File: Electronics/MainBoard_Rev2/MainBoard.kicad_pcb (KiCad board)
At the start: 2 copper layers, 57.2 x 35.1 mm, 70 parts, among them J1 Conn_01x04_Female, J2 DB9_Female, J3 USB_B_Micro, J4 Conn_01x04_Male, J5 Conn_01x02_Male, Q30 PMBT2222A, Q35 PMBT2222A, Q5 Q_NPN_BEC, Q6 Q_NPN_BEC, U1 ESP32-WROOM-32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

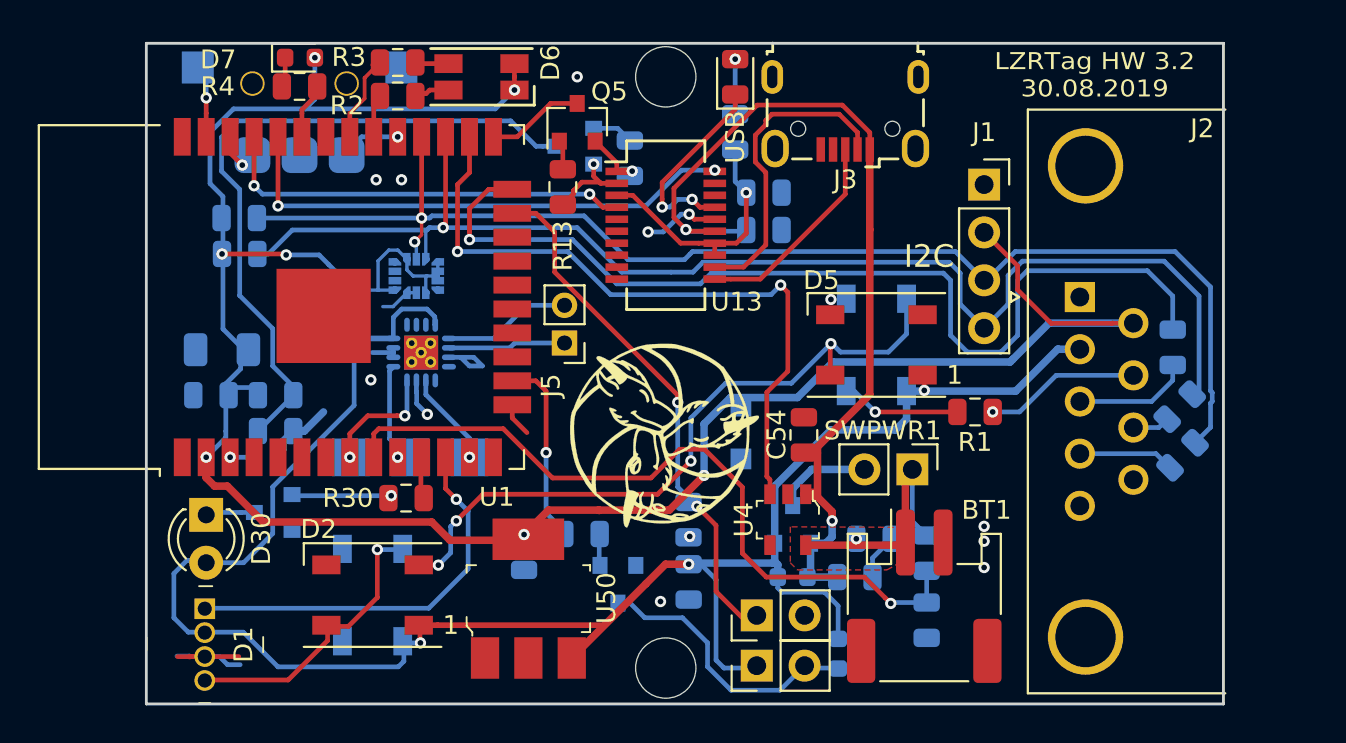
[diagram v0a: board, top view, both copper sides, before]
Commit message: Last changes for a functional Lasertag, ordered!
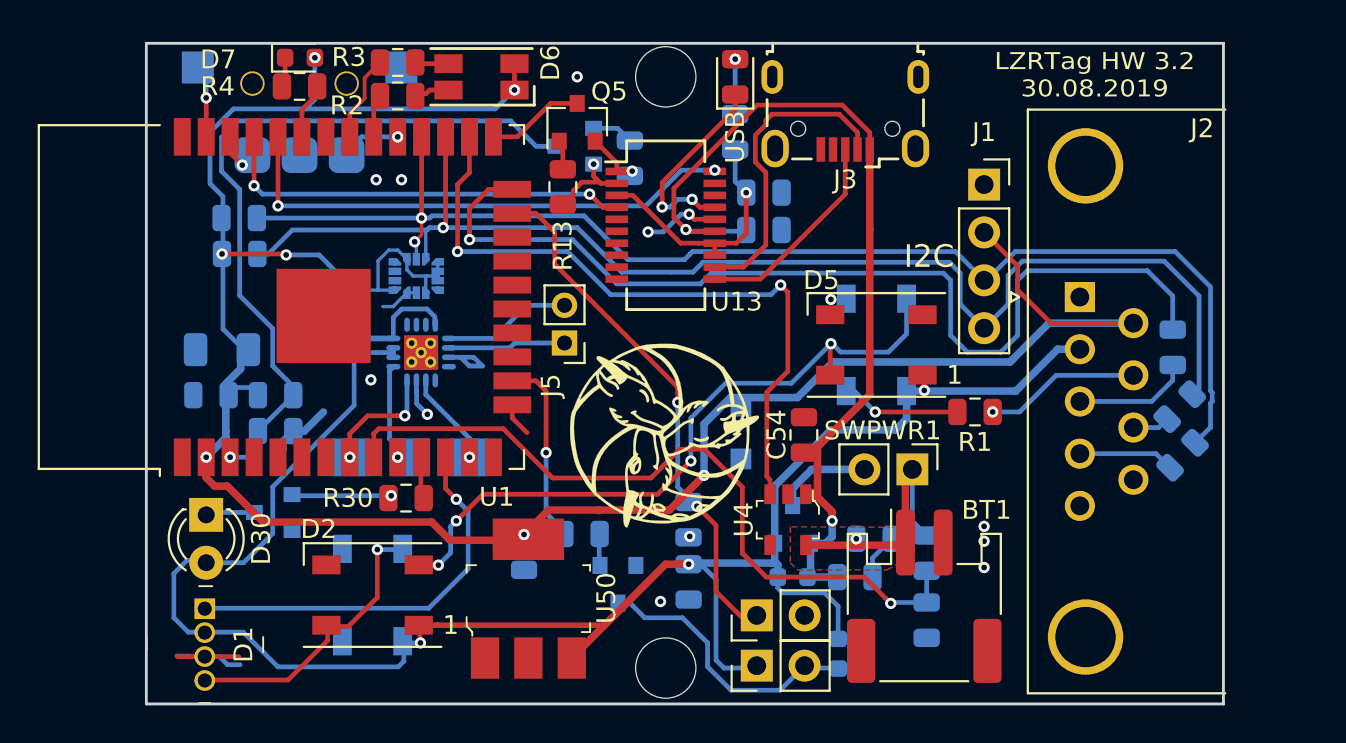
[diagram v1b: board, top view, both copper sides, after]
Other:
- rule trace_min: 0.2 -> 0.15
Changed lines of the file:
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@@
     (thickness 1.6)
     (drawings 17)
-    (tracks 581)
+    (tracks 583)
     (zones 0)
     (modules 70)
@@
     (zone_clearance 0.25)
     (zone_45_only yes)
-    (trace_min 0.2)
+    (trace_min 0.15)
     (segment_width 0.2)
     (edge_width 0.15)
@@
       (effects (font (size 0.5 0.5) (thickness 0.08)) (justify mirror))
     )
-    (pad 1 smd roundrect (at -0.9375 0 45) (size 0.975 1.4) (layers B.Cu B.Paste B.Mask) (roundrect_rratio 0.25)
+    (pad 1 smd roundrect (at -0.937501 0 45) (size 0.975 1.4) (layers B.Cu B.Paste B.Mask) (roundrect_rratio 0.25)
       (net 83 "Net-(J2-Pad4)"))
-    (pad 2 smd roundrect (at 0.9375 0 45) (size 0.975 1.4) (layers B.Cu B.Paste B.Mask) (roundrect_rratio 0.25)
+    (pad 2 smd roundrect (at 0.937501 0 45) (size 0.975 1.4) (layers B.Cu B.Paste B.Mask) (roundrect_rratio 0.25)
       (net 53 SCL))
     (model ${KISYS3DMOD}/Resistor_SMD.3dshapes/R_0805_2012Metric.wrl
@@
   (via (at 72.441 80.01) (size 0.6) (drill 0.3) (layers F.Cu B.Cu) (net 5))
   (segment (start 67.7165 97.3075) (end 67.7165 98.425) (width 0.25) (layer B.Cu) (net 5))
-  (segment (start 67.7165 98.425) (end 67.7165 99.822) (width 0.25) (layer B.Cu) (net 5))
+  (segment (start 67.7165 98.425) (end 67.7165 99.822) (width 0.4) (layer B.Cu) (net 5))
+  (segment (start 67.7165 99.822) (end 67.7165 100.1685) (width 0.4) (layer B.Cu) (net 5))
+  (segment (start 67.7165 100.1685) (end 66.675 101.21) (width 0.4) (layer B.Cu) (net 5))
   (segment (start 67.9195 97.5105) (end 69.215 97.5105) (width 0.25) (layer B.Cu) (net 5))
   (segment (start 67.7165 97.3075) (end 67.9195 97.5105) (width 0.25) (layer B.Cu) (net 5))
-  (segment (start 67.7165 100.1685) (end 66.675 101.21) (width 0.25) (layer B.Cu) (net 5))
-  (segment (start 67.7165 99.822) (end 67.7165 100.1685) (width 0.25) (layer B.Cu) (net 5))
   (segment (start 114.73863 94.095) (end 114.72663 94.107) (width 0.25) (layer F.Cu) (net 5))
   (segment (start 115.87 94.095) (end 114.73863 94.095) (width 0.25) (layer F.Cu) (net 5))
@@
   (segment (start 68.1228 82.7278) (end 71.9328 82.7278) (width 0.25) (layer B.Cu) (net 5))
   (segment (start 66.8782 83.9724) (end 68.1228 82.7278) (width 0.25) (layer B.Cu) (net 5))
-  (segment (start 67.7165 97.3075) (end 68.5038 96.5202) (width 0.25) (layer B.Cu) (net 5))
+  (segment (start 67.7165 97.3075) (end 68.5038 96.5202) (width 0.4) (layer B.Cu) (net 5))
+  (segment (start 68.5038 96.5202) (end 68.5038 95.343399) (width 0.4) (layer B.Cu) (net 5))
   (segment (start 68.5038 95.343399) (end 67.564 94.403599) (width 0.25) (layer B.Cu) (net 5))
   (segment (start 71.9328 82.7278) (end 72.441 82.2196) (width 0.25) (layer B.Cu) (net 5))
-  (segment (start 68.5038 96.5202) (end 68.5038 95.343399) (width 0.25) (layer B.Cu) (net 5))
   (segment (start 67.564 94.403599) (end 67.564 87.376) (width 0.25) (layer B.Cu) (net 5))
   (segment (start 71.9328 82.7278) (end 82.0166 82.7278) (width 0.25) (layer B.Cu) (net 5))
@@
   (segment (start 99.822 99.7585) (end 103.251 99.7585) (width 0.4) (layer B.Cu) (net 26))
   (segment (start 103.251 99.7585) (end 103.835 99.1745) (width 0.4) (layer B.Cu) (net 26))
-  (segment (start 100.203 109.093) (end 100.203 110.8455) (width 0.25) (layer B.Cu) (net 26))
-  (segment (start 97.0025 107.569) (end 97.0025 108.144) (width 0.25) (layer B.Cu) (net 26))
-  (segment (start 97.0025 108.144) (end 97.22751 108.36901) (width 0.25) (layer B.Cu) (net 26))
-  (segment (start 99.47901 108.36901) (end 100.203 109.093) (width 0.25) (layer B.Cu) (net 26))
-  (segment (start 97.22751 108.36901) (end 99.47901 108.36901) (width 0.25) (layer B.Cu) (net 26))
   (segment (start 93.726 111.971) (end 94.15 112.395) (width 0.25) (layer B.Cu) (net 26))
   (segment (start 92.274592 106.823447) (end 92.291039 106.807) (width 0.25) (layer B.Cu) (net 26))
@@
   (segment (start 91.0457 106.8855) (end 90.0081 107.9231) (width 0.4) (layer F.Cu) (net 26))
   (segment (start 92.274592 106.8855) (end 91.0457 106.8855) (width 0.4) (layer F.Cu) (net 26))
+  (segment (start 100.203 109.1184) (end 100.203 110.8455) (width 0.25) (layer B.Cu) (net 26))
+  (segment (start 99.67861 108.59401) (end 100.203 109.1184) (width 0.25) (layer B.Cu) (net 26))
+  (segment (start 99.67516 108.59401) (end 99.67861 108.59401) (width 0.25) (layer B.Cu) (net 26))
+  (segment (start 97.0025 107.569) (end 97.0025 108.144) (width 0.25) (layer B.Cu) (net 26))
+  (segment (start 97.0025 108.144) (end 97.2657 108.4072) (width 0.25) (layer B.Cu) (net 26))
+  (segment (start 97.2657 108.4072) (end 99.48835 108.4072) (width 0.25) (layer B.Cu) (net 26))
+  (segment (start 99.48835 108.4072) (end 99.67516 108.59401) (width 0.25) (layer B.Cu) (net 26))
   (segment (start 98.298 112.395) (end 100.1775 112.395) (width 0.25) (layer B.Cu) (net 27))
   (segment (start 97.122999 113.570001) (end 98.298 112.395) (width 0.25) (layer B.Cu) (net 27))
@@
   (segment (start 84.709 100.965) (end 84.709 104.1655) (width 0.25) (layer B.Cu) (net 39))
   (via (at 91.694 98.297992) (size 0.6) (drill 0.3) (layers F.Cu B.Cu) (net 40))
-  (segment (start 91.694 97.917) (end 91.694 98.297992) (width 0.25) (layer F.Cu) (net 40))
-  (segment (start 82.915 88.265) (end 84.165 88.265) (width 0.25) (layer F.Cu) (net 40))
-  (segment (start 84.165 88.265) (end 85.1662 89.2662) (width 0.25) (layer F.Cu) (net 40))
-  (segment (start 85.1662 89.2662) (end 85.1662 91.3892) (width 0.25) (layer F.Cu) (net 40))
-  (segment (start 85.1662 91.3892) (end 91.694 97.917) (width 0.25) (layer F.Cu) (net 40))
   (segment (start 91.694 98.297992) (end 91.694 102.793802) (width 0.25) (layer B.Cu) (net 40))
   (segment (start 91.694 102.793802) (end 92.410001 103.509803) (width 0.25) (layer B.Cu) (net 40))
@@
   (segment (start 93.726 108.331) (end 93.726 104.825802) (width 0.25) (layer F.Cu) (net 40))
   (segment (start 95.25 109.855) (end 93.726 108.331) (width 0.25) (layer F.Cu) (net 40))
+  (segment (start 91.694 97.4979) (end 91.694 98.297992) (width 0.25) (layer F.Cu) (net 40))
+  (segment (start 82.915 88.265) (end 84.165 88.265) (width 0.25) (layer F.Cu) (net 40))
+  (segment (start 85.1662 89.2662) (end 85.1662 90.9701) (width 0.25) (layer F.Cu) (net 40))
+  (segment (start 84.165 88.265) (end 85.1662 89.2662) (width 0.25) (layer F.Cu) (net 40))
+  (segment (start 85.1662 90.9701) (end 91.694 97.4979) (width 0.25) (layer F.Cu) (net 40))
   (segment (start 78.53 81.726) (end 78.341 81.915) (width 0.25) (layer F.Cu) (net 41))
   (segment (start 79.53 81.726) (end 78.53 81.726) (width 0.25) (layer F.Cu) (net 41))

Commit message: Modify board for the v3.3 release-ish
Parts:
- removed D35: D_Schottky, Diode_SMD:D_0603_1608Metric
- removed D6: LED_Dual_AACC, LED_SMD:LED_RGB_1210
- removed D7: LED, LED_SMD:LED_0603_1608Metric
- removed J2: DB9_Female, Connector_Dsub:DSUB-9_Female_Horizontal_P2.77x2.84mm_EdgePinOffset4.94mm_Housed_MountingHolesOffset7.48mm
- removed Q35: PMBT2222A, Package_TO_SOT_SMD:SOT-23
- removed R2, R3: 220R, Resistor_SMD:R_0805_2012Metric
- removed R35: 2.2k, Resistor_SMD:R_0805_2012Metric
- removed R4: 220, Resistor_SMD:R_0805_2012Metric
- added C201: 0.1uF, Capacitor_SMD:C_0805_2012Metric, F.Cu at (85.4, 101.3)
- added C401: 1uF, Capacitor_SMD:C_0805_2012Metric, B.Cu at (109.6, 102.3)
- added D401: IN-PI42TAS, XasPrints:IN-PI42TAS, F.Cu at (109.1, 80.8)
- added D402: IN-PI42TAS, XasPrints:IN-PI42TAS, F.Cu at (116.6, 80.9)
- added J101: 54602-908LF, Connector_RJ:RJ45_Amphenol_54602-x08_Horizontal, F.Cu at (111.0, 99.7)
- added U401: DRV2605, Package_SO:VSSOP-10_3x3mm_P0.5mm, B.Cu at (111.5, 107.2)
- BT1: footprint Connector_JST:JST_PH_S2B-PH-SM4-TB_1x02-1MP_P2.00mm_Horizontal -> Connector_PinHeader_2.54mm:PinHeader_1x02_P2.54mm_Horizontal; moved to B.Cu
- C2, C31, C8: value 150nF -> 100nF
- C3: value 0.1uF -> 100nF
- D1: footprint digikey-footprints:LED_RGB_WP154A4SUREQBFZGC -> Connector_PinHeader_2.00mm:PinHeader_1x04_P2.00mm_Vertical
- D30: value SFH4346 -> SFH4545; footprint LED_THT:LED_D3.0mm_IRBlack -> Connector_PinHeader_2.00mm:PinHeader_1x02_P2.00mm_Vertical
- R1: value 220 -> 220R; moved to B.Cu
- R13, R14: value R_Small -> 10k
- R30, R7, R8, R9: value 220 -> 220R
- R55: value 100k -> 50k
- R56: value 200k -> 50k; moved to F.Cu
- U3: value LSM6DS3 -> LSM6DSMTR
- moved H4 27.5 mm to (100.6, 83.9), turned to 0 degrees
- moved H3 22.2 mm to (87.4, 103.5)
- moved J1 19.9 mm to (116.6, 104.6)
- moved VBR1 17.9 mm to (113.7, 112.2), turned to 270 degrees
- moved R7 13.9 mm to (105.0, 90.5), turned to 180 degrees
- moved R8 11.3 mm to (111.3, 89.7), turned to 0 degrees
- moved R9 10.2 mm to (113.7, 92.0), turned to 0 degrees
- moved R1 7.52 mm to (113.7, 94.6), turned to 0 degrees
- moved R56 5.21 mm to (105.9, 104.7), turned to 0 degrees
- moved D1 4.72 mm to (65.2, 106.6), turned to 0 degrees
- moved D30 2.67 mm to (67.9, 106.6), turned to 0 degrees
- moved R55 1.83 mm to (105.9, 104.7), turned to 180 degrees
- moved BT1 1.26 mm to (103.9, 107.6), turned to 270 degrees
- moved H6 0.56 mm to (91.1, 99.5)
- moved SWPWR1 0.10 mm to (104.2, 101.9)
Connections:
- AMP1 pad 7: Net-(AMP1-Pad7) -> +BATT
- BT1 pad 1: /PowerHandling/B_Raw+ -> Net-(BT1-Pad1)
- C53 pad 1: /PowerHandling/B_Raw+ -> Net-(BT1-Pad1)
- D4 pad 2: /LED_2 -> Net-(D4-Pad2)
- QPWR1 pad 3: Net-(QPWR1-Pad3) -> /PowerHandling/B_Raw+
- SWPWR1 pad 1: /PowerHandling/B_Raw+ -> Net-(BT1-Pad1)
- SWPWR1 pad 2: Net-(QPWR1-Pad3) -> /PowerHandling/B_Raw+
- U1 pad 16: /VBRT -> Net-(U1-Pad16)
- U1 pad 30: /CHG_R -> Net-(U1-Pad30)
- U1 pad 31: /CHG_G -> Net-(U1-Pad31)
- U1 pad 33: /CONN_IND -> Net-(U1-Pad33)
- U1 pad 39: (no net) -> GND
- U4 pad 5: /PowerHandling/B_Raw+ -> Net-(BT1-Pad1)
- U50 pad 2: Net-(U50-Pad2) -> +3V3
- VBR1 pad 1: +BATT -> Net-(U401-Pad7)
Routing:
- net +BATT: track 106.8 -> 130.8 mm, vias 3 -> 8
- net /IR_IN: track 52.1 -> 29.3 mm
- net +3V3: track 129.1 -> 109.3 mm, vias 7 -> 6
- net Net-(D401-Pad2): track 0.00 -> 18.5 mm, vias 0 -> 2
- net Net-(D401-Pad4): track 0.00 -> 18.1 mm, vias 0 -> 2
- net SDA: track 69.0 -> 82.5 mm, vias 1 -> 3
- net SCL: track 69.3 -> 82.2 mm, vias 2 -> 4
- net Net-(U401-Pad9): track 14.8 -> 2.91 mm
- net /VBRT: track 10.2 -> 0.00 mm, vias 1 -> 0
- net /LED_2: track 6.35 -> 15.4 mm
- net Net-(BT1-Pad1): track 0.00 -> 8.76 mm, vias 0 -> 1
- net Net-(J101-Pad5): track 8.27 -> 1.75 mm, vias 1 -> 0
- net /V_SENSE: track 39.6 -> 44.8 mm
- net /CHG_G: track 5.15 -> 0.00 mm
- net Net-(QPWR1-Pad3): track 5.14 -> 0.00 mm
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- added copper zone on F.Cu, net Net-(BT1-Pad1)
- removed copper zone on F.Cu, net /PowerHandling/B_Raw+
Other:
- board text added: "-IR"
- board text added: "AMMO"
- board text added: "BAT"
- board text added: "HP"
- board text added: "LZRTag HW 3.3 21.06.2021"
- board text added: "Neo Out"
- board text added: "Neo in"
- board text removed: "LZRTag HW 3.2 30.08.2019"
